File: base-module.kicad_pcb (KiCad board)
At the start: 2 copper layers, 111 parts, among them J200 09031967921, Q700 S9013, U300 TPS563201DDCR, U301 TPS563201DDCR, U402 TS3USB30ERSWR, U403 IP4234CZ6,115, U404 IP4234CZ6,115, U406 CH334R, U407 STM32F750V8Tx, U501 TJA1044GTK_3Z, U602 TJA1044GTK_3Z, U700 STM32F103CBTx, X402 X322512MSB4SI, X700 X50328MSB2GI, Y403 12Mhz

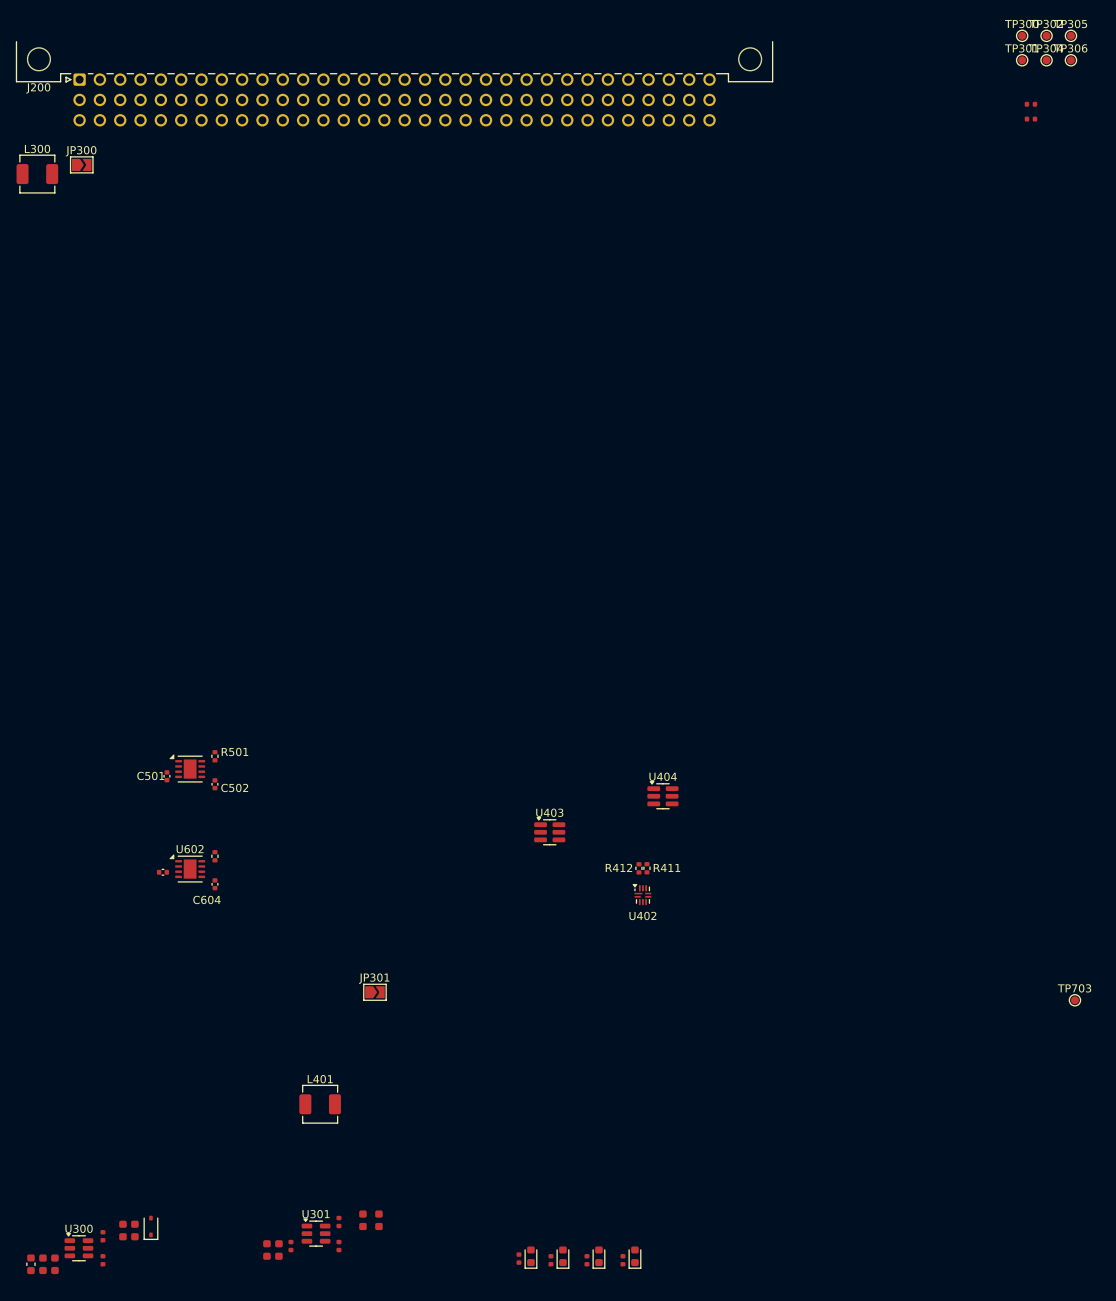
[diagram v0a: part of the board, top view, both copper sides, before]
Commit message: [2] Update converter layout
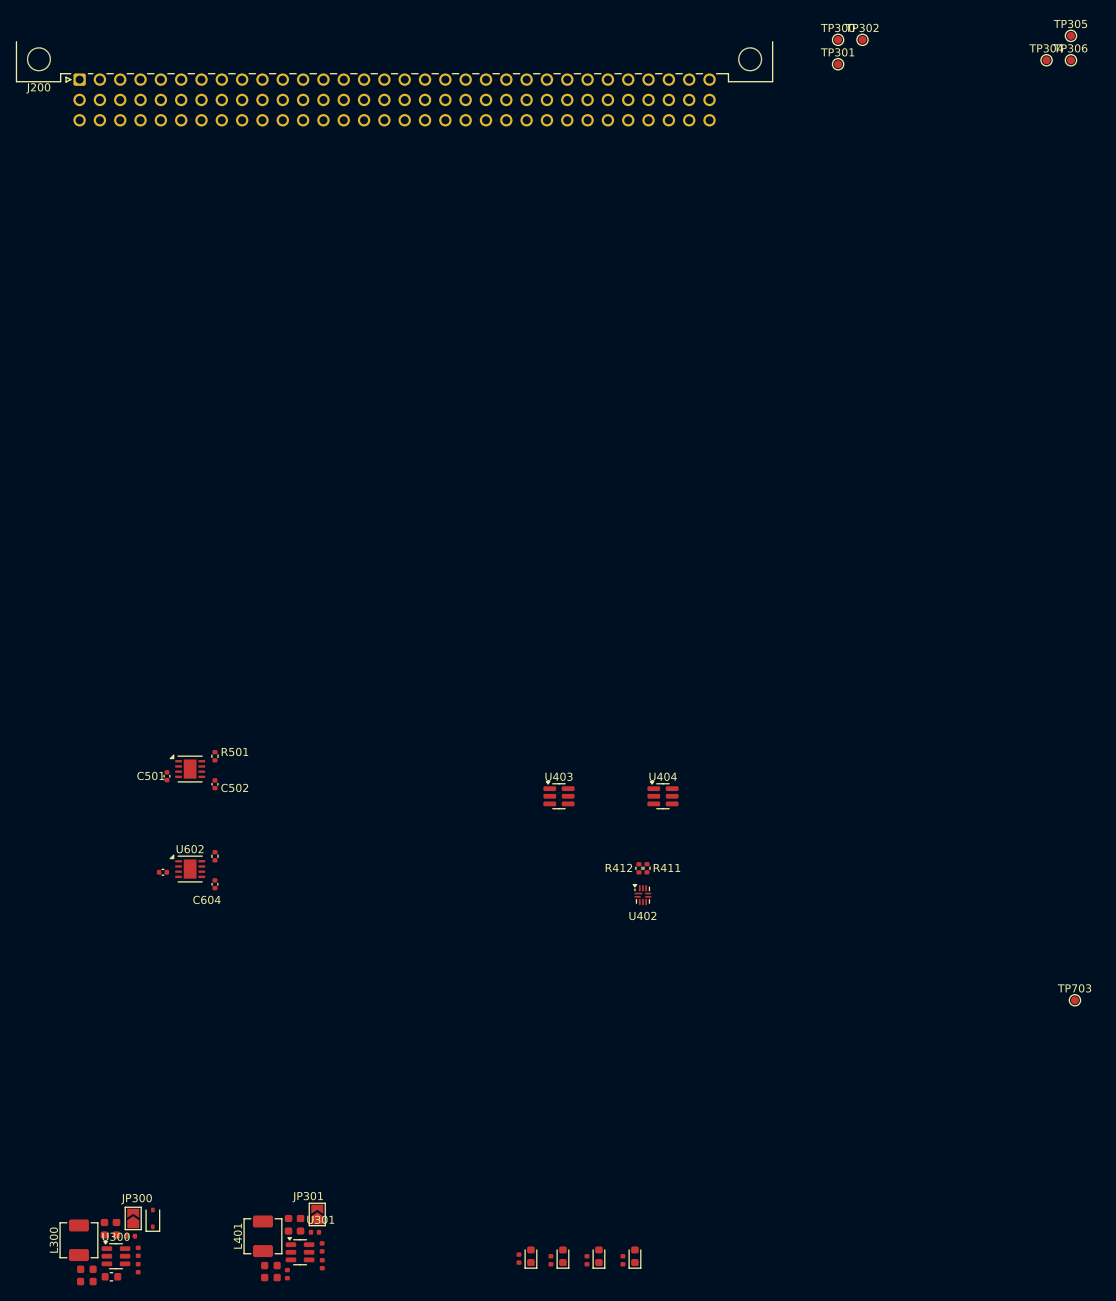
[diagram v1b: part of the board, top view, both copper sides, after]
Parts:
- moved R300 181.7 mm to (32.9, 177.4), turned to -90 degrees
- moved R302 166.6 mm to (55.9, 176.9), turned to -90 degrees
- moved L300 133.4 mm to (25.5, 176.0), turned to 90 degrees
- moved JP300 131.8 mm to (32.3, 173.3), turned to 90 degrees
- moved JP301 28.7 mm to (55.3, 172.8), turned to 90 degrees
- moved TP300 23.0 mm to (120.4, 25.9)
- moved TP301 23.0 mm to (120.4, 29.0)
- moved TP302 23.0 mm to (123.4, 25.9)
- moved L401 18.0 mm to (48.5, 175.5), turned to 90 degrees
- moved C306 11.3 mm to (51.7, 174.1), turned to -90 degrees
- moved F300 10.2 mm to (29.6, 180.6), turned to 180 degrees
- moved C307 7.82 mm to (53.2, 174.1), turned to -90 degrees
- moved C304 5.53 mm to (26.5, 179.6), turned to 180 degrees
- moved U300 4.74 mm to (30.1, 178.0)
- moved U403 4.64 mm to (85.5, 120.5)
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
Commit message: [2] Add JLC4161H stackup
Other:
- copper layers 2 -> 4
- board text added: "0"
- board text added: "0 mm"
- board text added: "0.01 mm"
- board text added: "0.0152 mm"
- board text added: "0.02"
- board text added: "0.035 mm"
- board text added: "0.2104 mm"
- board text added: "1"
- board text added: "1.065 mm"
- board text added: "3.3"
- board text added: "4.4"
- board text added: "4.6"
- board text added: "B.Cu"
- board text added: "B.Mask"
- board text added: "B.Paste"
- board text added: "B.Silkscreen"
- board text added: "Black"
- board text added: "Bottom Silk Screen"
- board text added: "Bottom Solder Mask"
- board text added: "Bottom Solder Paste"
- board text added: "Color"
- board text added: "Dielectric 1"
- board text added: "Dielectric 2"
- board text added: "Dielectric 3"
- board text added: "Epsilon R"
- board text added: "F.Cu"
- board text added: "F.Mask"
- board text added: "F.Paste"
- board text added: "F.Silkscreen"
- board text added: "FR4"
- board text added: "FR4 natural"
- board text added: "In1.Cu"
- board text added: "In2.Cu"
- board text added: "Layer Name"
- board text added: "Loss Tangent"
- board text added: "Material"
- board text added: "Not specified"
- board text added: "Thickness (mm)"
- board text added: "Top Silk Screen"
- board text added: "Top Solder Mask"
- board text added: "Top Solder Paste"
- board text added: "Type"
- board text added: "White"
- board text added: "copper"
- board text added: "core"
- board text added: "prepreg"

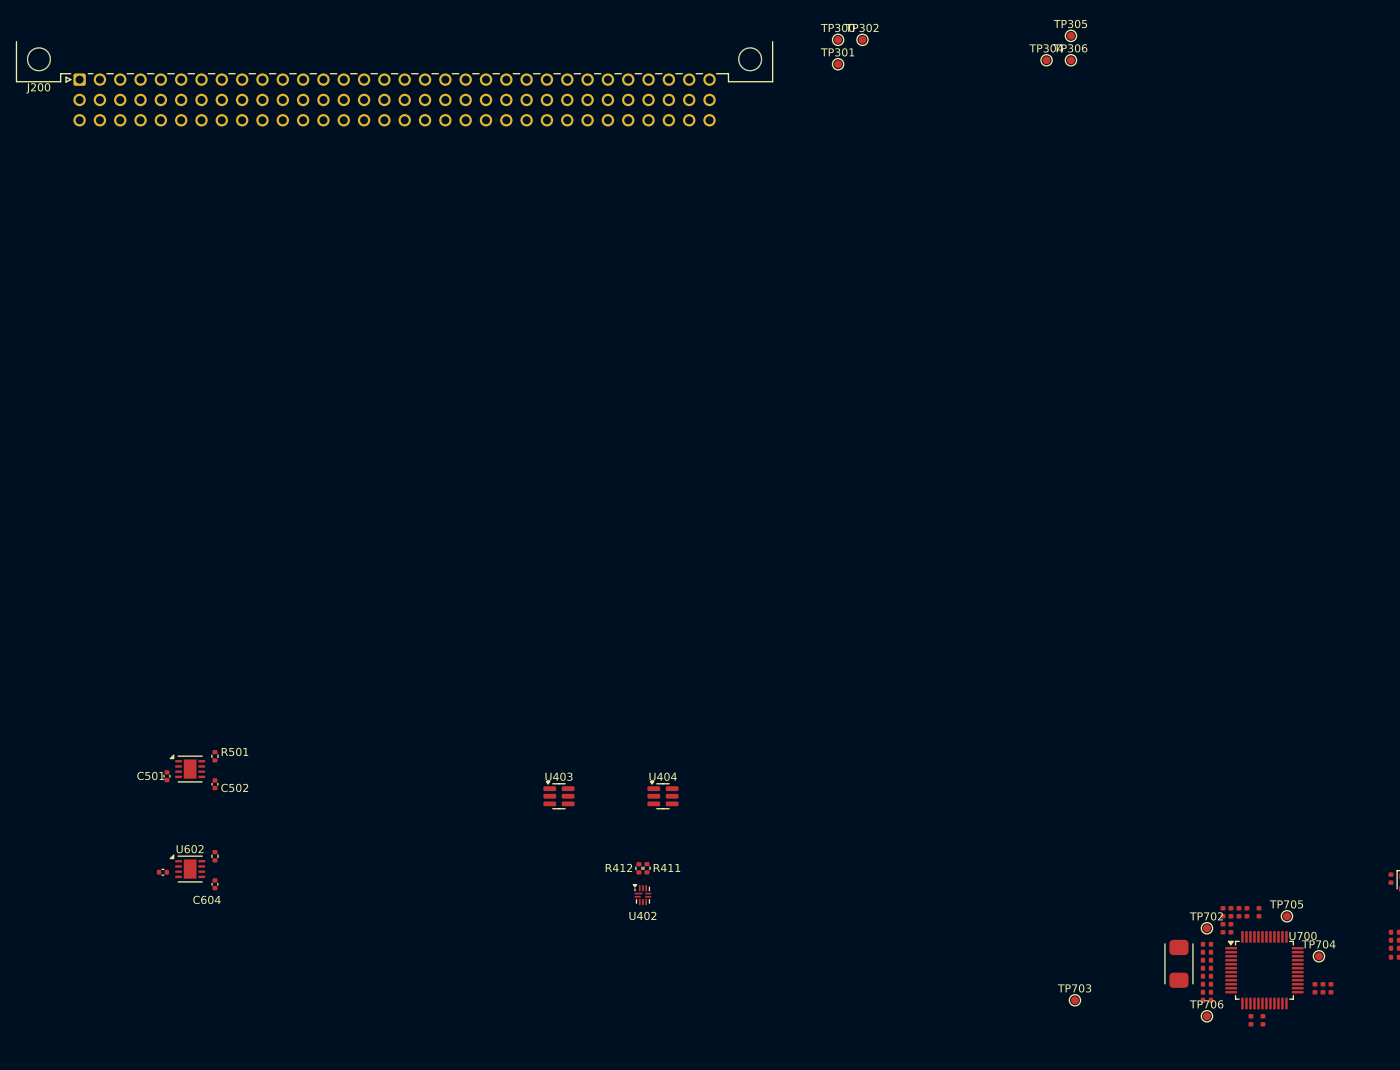
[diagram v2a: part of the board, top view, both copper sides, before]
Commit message: [2] Setup pre-defined track widths and via sizes, start ST-LINK layout
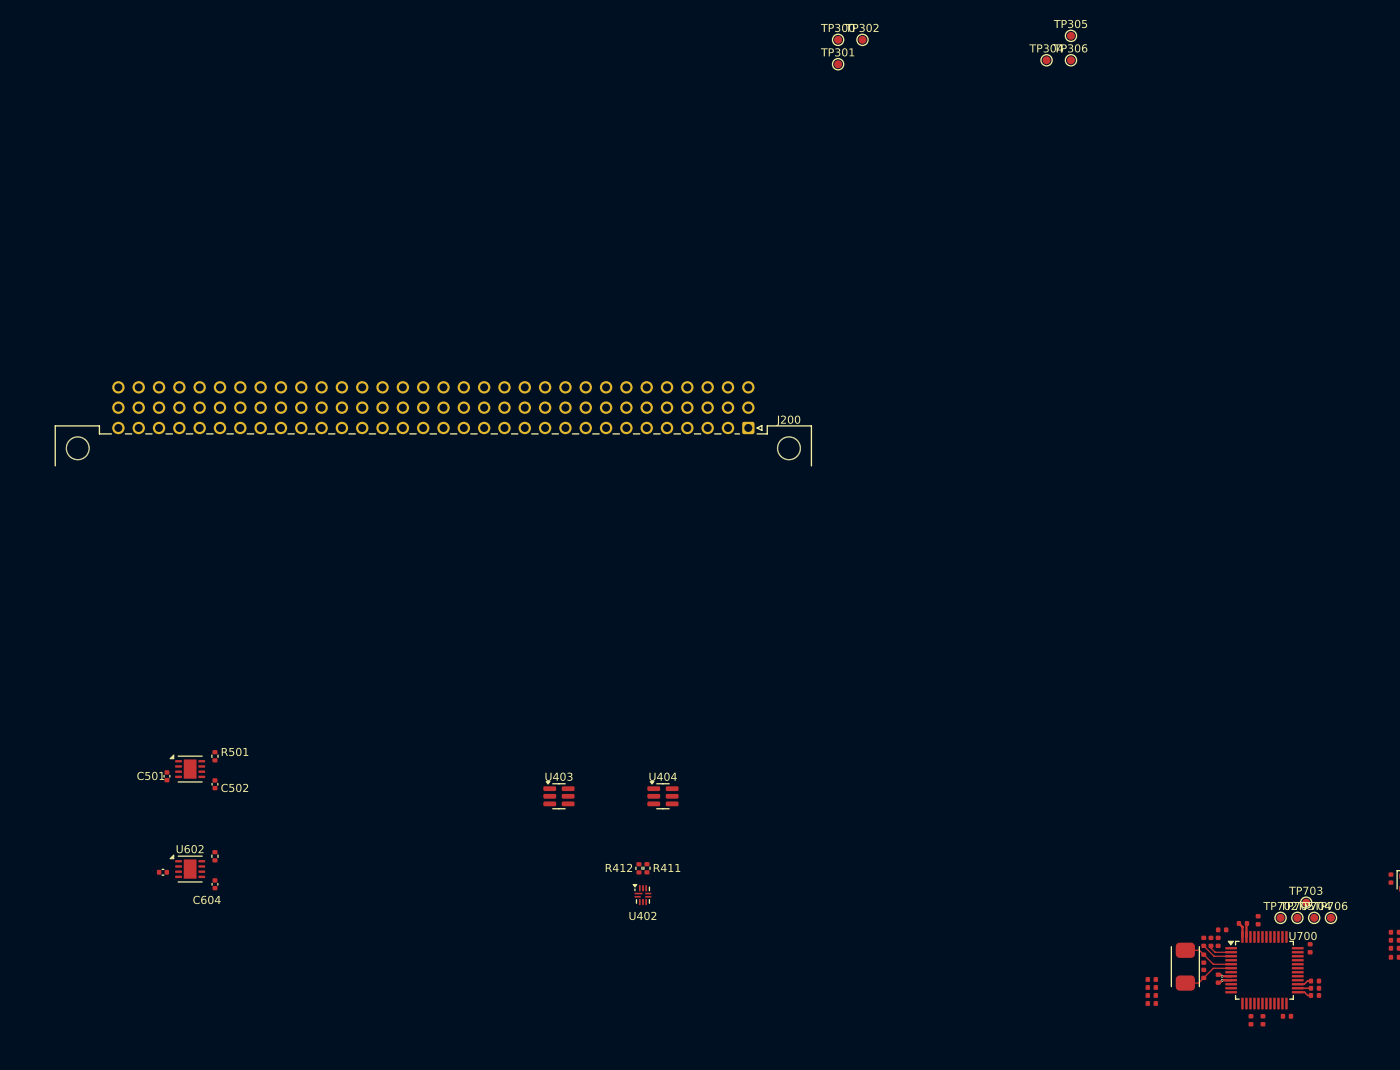
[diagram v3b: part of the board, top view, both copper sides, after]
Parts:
- moved J200 94.3 mm to (109.2, 74.5), turned to 180 degrees
- moved TP703 31.4 mm to (178.9, 133.8)
- moved TP706 19.8 mm to (182.0, 135.7)
- moved C703 15.3 mm to (176.5, 148.0), turned to 180 degrees
- moved C705 9.97 mm to (179.4, 139.5), turned to -90 degrees
- moved TP702 9.29 mm to (175.7, 135.7)
- moved C704 8.45 mm to (167.9, 143.3)
- moved C706 6.91 mm to (159.6, 143.4)
- moved R700 6.91 mm to (159.6, 144.4)
- moved R701 6.91 mm to (159.6, 145.4)
- moved R703 6.91 mm to (159.6, 146.4)
- moved TP704 4.84 mm to (179.9, 135.7)
- moved C700 3.80 mm to (168.4, 137.2), turned to 180 degrees
- moved C702 2.57 mm to (171.0, 136.4), turned to 0 degrees
- moved C701 2.33 mm to (167.9, 138.7), turned to 90 degrees
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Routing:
- net /ST-LINK/STLINK-OSC_OUT: track 0.00 -> 6.49 mm
- net /ST-LINK/STLINK-OSC_IN: track 0.00 -> 6.45 mm
- net Net-(U700-PC14): track 0.00 -> 3.99 mm
- net +3V3: track 0.00 -> 3.62 mm, vias 0 -> 1
- net GND: track 0.00 -> 3.42 mm, vias 0 -> 1
- net Net-(U700-PC13): track 0.00 -> 3.02 mm
- net Net-(U700-PB14): track 0.00 -> 1.82 mm
- net Net-(U700-PB12): track 0.00 -> 1.82 mm
- net Net-(U700-PB13): track 0.00 -> 1.65 mm

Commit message: [2] Improve layout
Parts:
- added TP300: TestPoint, TestPoint:TestPoint_Pad_D1.0mm, F.Cu at (69.0, 96.8)
- added TP301: TestPoint, TestPoint:TestPoint_Pad_D1.0mm, F.Cu at (64.1, 104.8)
- added TP302: TestPoint, TestPoint:TestPoint_Pad_D1.0mm, F.Cu at (69.1, 104.8)
- added TP304: TestPoint, TestPoint:TestPoint_Pad_D1.0mm, F.Cu at (85.1, 96.5)
- added TP305: TestPoint, TestPoint:TestPoint_Pad_D1.0mm, F.Cu at (85.1, 104.5)
- added TP306: TestPoint, TestPoint:TestPoint_Pad_D1.0mm, F.Cu at (80.1, 104.5)
- moved C303 93.4 mm to (65.8, 96.4), turned to 90 degrees
- moved C304 92.6 mm to (67.2, 96.4), turned to 90 degrees
- moved F300 90.9 mm to (63.5, 96.2), turned to 0 degrees
- moved C309 90.5 mm to (81.8, 96.1), turned to 90 degrees
- moved C308 89.6 mm to (83.2, 96.1), turned to 90 degrees
- moved C310 88.7 mm to (80.1, 96.2), turned to 180 degrees
- moved R301 86.6 mm to (60.2, 97.3), turned to 90 degrees
- moved R303 86.4 mm to (59.3, 94.5), turned to 180 degrees
- moved L300 86.2 mm to (67.6, 100.8), turned to -90 degrees
- moved D301 85.9 mm to (61.8, 94.5), turned to 0 degrees
- moved U300 85.7 mm to (62.9, 98.8), turned to 180 degrees
- moved R307 84.5 mm to (76.2, 97.0), turned to 90 degrees
- moved R304 84.4 mm to (82.0, 94.2), turned to 0 degrees
- moved D302 83.9 mm to (79.5, 94.3), turned to 180 degrees
- moved U301 83.1 mm to (79.0, 98.5), turned to 180 degrees
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
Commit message: [2] Change layout
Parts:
- moved Y403 88.1 mm to (135.0, 96.5), turned to 0 degrees
- moved C438 86.1 mm to (136.7, 102.7), turned to 90 degrees
- moved C426 85.3 mm to (137.6, 99.7), turned to -90 degrees
- moved R443 85.1 mm to (126.5, 101.0)
- moved R444 85.1 mm to (126.5, 102.0)
- moved R445 85.1 mm to (126.5, 103.0)
- moved R446 85.1 mm to (126.5, 104.0)
- moved U406 85.1 mm to (132.0, 101.0)
- moved C439 84.7 mm to (138.2, 102.7), turned to 90 degrees
- moved C422 83.6 mm to (139.1, 99.7), turned to -90 degrees
- moved C436 80.5 mm to (136.3, 100.0), turned to -90 degrees
- moved TP304 52.2 mm to (33.0, 98.0)
- moved TP305 51.8 mm to (33.5, 100.0)
- moved TP306 46.7 mm to (33.5, 102.0)
- moved TP300 36.0 mm to (33.0, 96.0)
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
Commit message: [2] Group more elements
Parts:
- removed TP300 (x2), TP301 (x2), TP302 (x2), TP304 (x2), TP305 (x2), TP306 (x2): TestPoint, TestPoint:TestPoint_Pad_D1.0mm
- added C406: 100nF, PCM_JLCPCB:C_0402, F.Cu at (99.4, 124.2)
- added C407: 10uF, PCM_JLCPCB:C_0402, F.Cu at (97.3, 137.0)
- added C414: 100nF, PCM_JLCPCB:C_0402, F.Cu at (94.7, 137.0)
- added C415: 2.2uF, PCM_JLCPCB:C_0402, F.Cu at (116.8, 127.0)
- added C419: 2.2uF, PCM_JLCPCB:C_0402, F.Cu at (113.0, 141.8)
- added FB401: ~, PCM_JLCPCB:FB_0603, F.Cu at (96.0, 137.6)
- C401, C410: value 4u7 -> 100nF; footprint Capacitor_SMD:C_0402_1005Metric -> PCM_JLCPCB:C_0402
- C402, C403, C404: footprint Capacitor_SMD:C_0402_1005Metric -> PCM_JLCPCB:C_0402
- C405, C411: value 100nF -> 10uF; footprint Capacitor_SMD:C_0402_1005Metric -> PCM_JLCPCB:C_0402
- U501, U602: footprint HVSON-8-EP(3x3):HVSON-8-1EP_3x3mm_P0.65mm_EP1.6x2.4mm -> Package_SON:HVSON-8-1EP_3x3mm_P0.65mm_EP1.6x2.4mm
- moved C411 141.9 mm to (94.7, 138.9)
- moved C401 139.5 mm to (99.5, 122.3), turned to 90 degrees
- moved C408 138.5 mm to (90.6, 142.5)
- moved C413 138.5 mm to (96.1, 142.5)
- moved X402 138.5 mm to (93.4, 142.5)
- moved C412 137.1 mm to (104.3, 122.4)
- moved C409 137.0 mm to (98.0, 132.3)
- moved U407 137.0 mm to (107.5, 132.5)
- moved C410 136.6 mm to (98.3, 137.0)
- moved C403 136.5 mm to (101.5, 122.3), turned to 90 degrees
- moved C405 136.5 mm to (100.5, 124.2), turned to -90 degrees
- moved C402 135.5 mm to (100.5, 122.3), turned to 90 degrees
- moved C404 133.6 mm to (102.5, 122.3)
- moved R707 127.5 mm to (67.8, 138.3), turned to 0 degrees
- moved D700 125.9 mm to (67.7, 136.3), turned to -90 degrees
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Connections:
- net /MCU/PB7 renamed /MCU/BOOT_EN
- C401 pad 1: GND -> +3V3
- C401 pad 2: +3V3 -> GND
- C402 pad 1: GND -> +3V3
- C402 pad 2: +3V3 -> GND
- C403 pad 1: GND -> +3V3
- C403 pad 2: +3V3 -> GND
- C404 pad 1: GND -> +3V3
- C404 pad 2: +3V3 -> GND
- C405 pad 1: GND -> +3V3
- C405 pad 2: +3V3 -> GND
- C410 pad 1: GND -> Net-(U407-VDDA)
- C410 pad 2: Net-(U407-VDDA) -> GND
- C411 pad 1: GND -> +3V3
- C411 pad 2: +3V3 -> GND
- J200 pad b5: /Backplane/CAN1.+ -> /Backplane/CAN1..+
- J200 pad b6: /Backplane/CAN1.- -> /Backplane/CAN1..-
- J200 pad b8: /Backplane/CAN2.+ -> /Backplane/CAN2..+
- J200 pad b9: /Backplane/CAN2.- -> /Backplane/CAN2..-
- J200 pad c5: /Backplane/CAN1.+ -> /Backplane/CAN1..+
- J200 pad c6: /Backplane/CAN1.- -> /Backplane/CAN1..-
- J200 pad c8: /Backplane/CAN2.+ -> /Backplane/CAN2..+
- J200 pad c9: /Backplane/CAN2.- -> /Backplane/CAN2..-
- R712 pad 2: /ST-LINK/USB_D+ -> /ST-LINK/USB.D+
- TP703 pad 1: /ST-LINK/BOOT -> /ST-LINK/STLINK-BOOT0
- U407 pad 6: unconnected-(U407-VBAT-Pad6) -> +3V3
- U407 pad 81: /MCU/PD0 -> /MCU/CAN1.RX
- U407 pad 82: /MCU/PD1 -> /MCU/CAN1.TX
- U407 pad 91: /MCU/PB5 -> /MCU/CAN2.RX
- U407 pad 92: /MCU/PB6 -> /MCU/CAN2.TX
- U407 pad 95: /MCU/PB8 -> /MCU/I2C1.SCL
- U407 pad 96: /MCU/PB9 -> /MCU/I2C1.SCL
- U501 pad 1: /MCU/CAN transceiver 1/TX -> /MCU/CAN1.TX
- U501 pad 4: /MCU/CAN transceiver 1/RX -> /MCU/CAN1.RX
- U501 pad 6: /Backplane/CAN.1- -> /Backplane/CAN1.-
- U501 pad 7: /Backplane/CAN.1+ -> /Backplane/CAN1.+
- U602 pad 1: /MCU/CAN transceiver 2/TX -> /MCU/CAN2.TX
- U602 pad 4: /MCU/CAN transceiver 2/RX -> /MCU/CAN2.RX
- U602 pad 6: /Backplane/CAN.2- -> /Backplane/CAN2.-
- U602 pad 7: /Backplane/CAN.2+ -> /Backplane/CAN2.+
